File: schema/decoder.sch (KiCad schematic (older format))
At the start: 19 parts, among them Q1 BC177, U1 7402, U2 HEF4526B, U3 TLC555

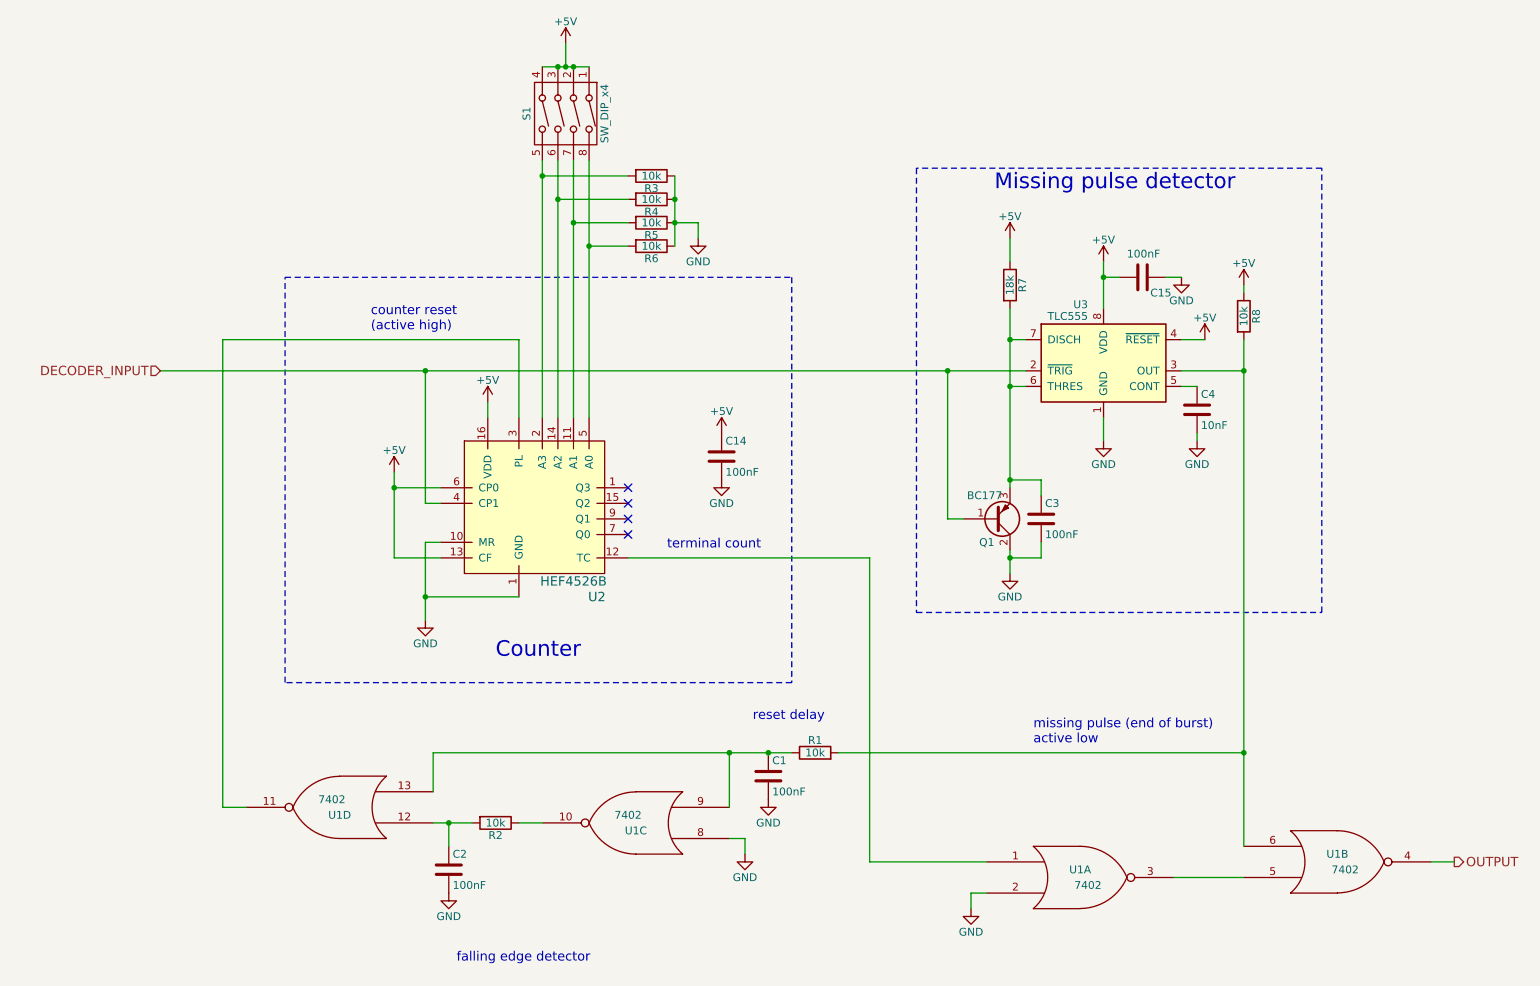
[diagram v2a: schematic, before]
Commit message: Add missing decoupling capacitors
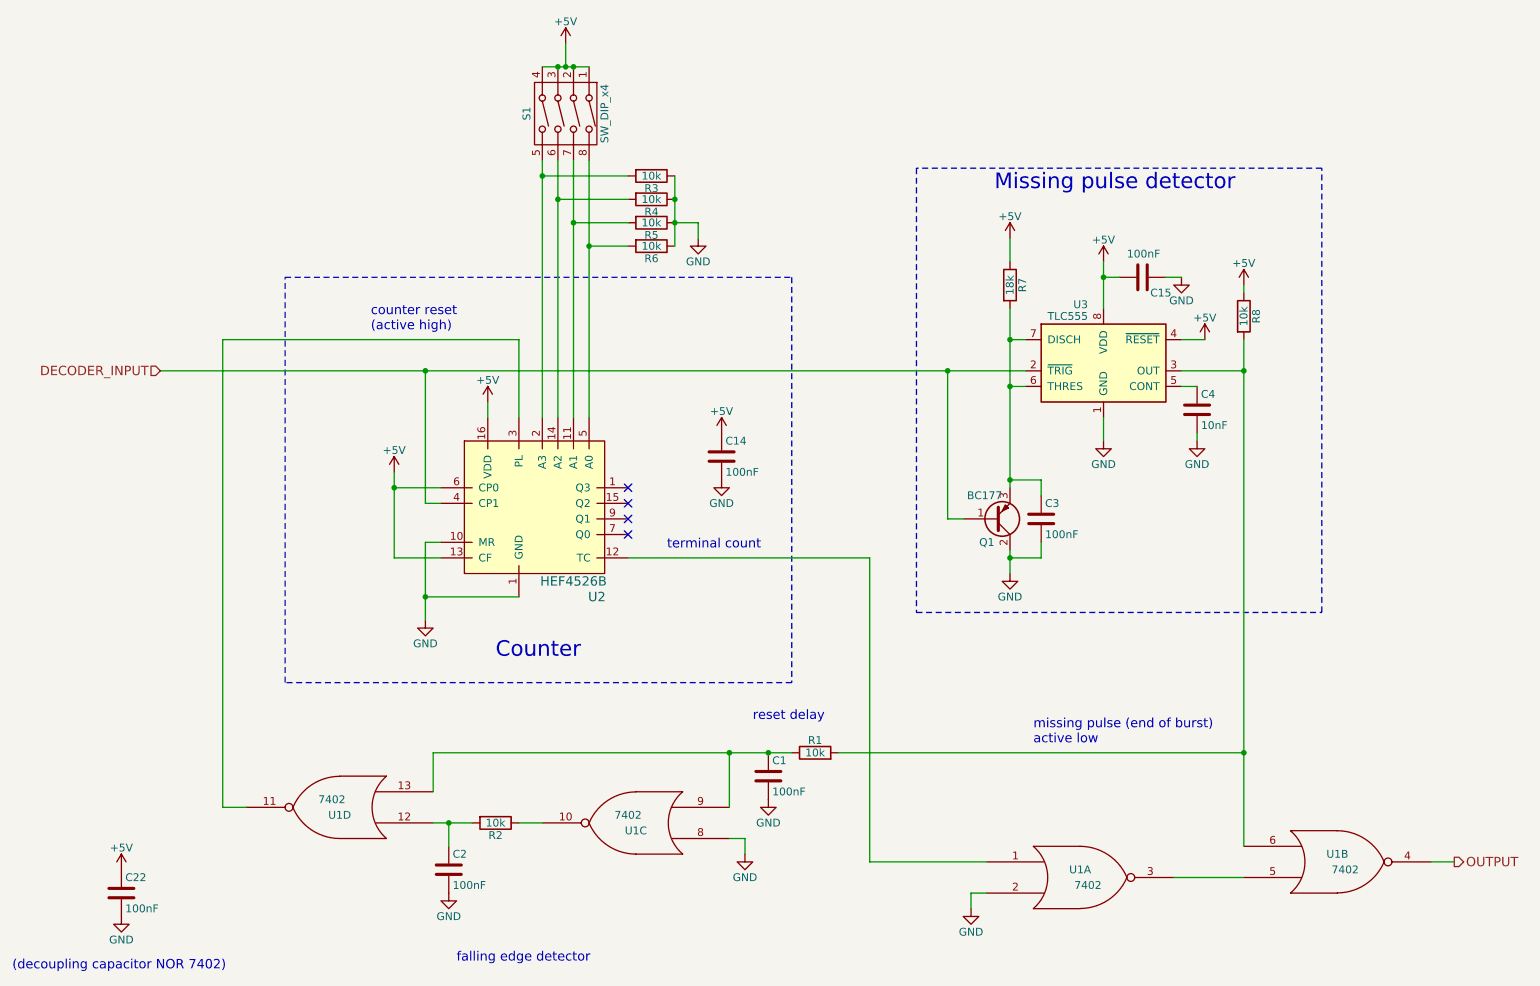
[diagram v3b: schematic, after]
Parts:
- added C22: 100nF, symbol C
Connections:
- net +5V: now also C22.1
- net GND: now also C22.2
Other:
- note added: "(decoupling capacitor NOR 7402)"
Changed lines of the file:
@@
 $EndComp
 $Comp
-L GND #PWR35
+L GND #PWR40
 U 1 1 58C0583B
 P 3350 4500
-F 0 "#PWR35" H 3350 4250 50  0001 C CNN
+F 0 "#PWR40" H 3350 4250 50  0001 C CNN
 F 1 "GND" H 3350 4350 50  0000 C CNN
 F 2 "" H 3350 4500 50  0000 C CNN
@@
 $EndComp
 $Comp
-L +5V #PWR38
+L +5V #PWR43
 U 1 1 58C05885
 P 4250 800
-F 0 "#PWR38" H 4250 650 50  0001 C CNN
+F 0 "#PWR43" H 4250 650 50  0001 C CNN
 F 1 "+5V" H 4250 940 50  0000 C CNN
 F 2 "" H 4250 800 50  0000 C CNN
@@
 $EndComp
 $Comp
-L GND #PWR44
+L GND #PWR49
 U 1 1 58C05E32
 P 6850 6350
-F 0 "#PWR44" H 6850 6100 50  0001 C CNN
+F 0 "#PWR49" H 6850 6100 50  0001 C CNN
 F 1 "GND" H 6850 6200 50  0000 C CNN
 F 2 "" H 6850 6350 50  0000 C CNN
@@
 $EndComp
 $Comp
-L GND #PWR48
+L GND #PWR53
 U 1 1 58C061DE
 P 7700 3350
-F 0 "#PWR48" H 7700 3100 50  0001 C CNN
+F 0 "#PWR53" H 7700 3100 50  0001 C CNN
 F 1 "GND" H 7700 3200 50  0000 C CNN
 F 2 "" H 7700 3350 50  0000 C CNN
@@
 $EndComp
 $Comp
-L GND #PWR46
+L GND #PWR51
 U 1 1 58C0698F
 P 7100 4200
-F 0 "#PWR46" H 7100 3950 50  0001 C CNN
+F 0 "#PWR51" H 7100 3950 50  0001 C CNN
 F 1 "GND" H 7100 4050 50  0000 C CNN
 F 2 "" H 7100 4200 50  0000 C CNN
@@
 $EndComp
 $Comp
-L GND #PWR50
+L GND #PWR55
 U 1 1 58C06B39
 P 8300 3350
-F 0 "#PWR50" H 8300 3100 50  0001 C CNN
+F 0 "#PWR55" H 8300 3100 50  0001 C CNN
 F 1 "GND" H 8300 3200 50  0000 C CNN
 F 2 "" H 8300 3350 50  0000 C CNN
@@
 $EndComp
 $Comp
-L GND #PWR42
+L GND #PWR47
 U 1 1 58C07F5B
 P 5400 6000
-F 0 "#PWR42" H 5400 5750 50  0001 C CNN
+F 0 "#PWR47" H 5400 5750 50  0001 C CNN
 F 1 "GND" H 5400 5850 50  0000 C CNN
 F 2 "" H 5400 6000 50  0000 C CNN
@@
 $EndComp
 $Comp
-L GND #PWR36
+L GND #PWR41
 U 1 1 58C08807
 P 3500 6250
-F 0 "#PWR36" H 3500 6000 50  0001 C CNN
+F 0 "#PWR41" H 3500 6000 50  0001 C CNN
 F 1 "GND" H 3500 6100 50  0000 C CNN
 F 2 "" H 3500 6250 50  0000 C CNN
@@
 $EndComp
 $Comp
-L GND #PWR43
+L GND #PWR48
 U 1 1 58C08D75
 P 5550 5650
-F 0 "#PWR43" H 5550 5400 50  0001 C CNN
+F 0 "#PWR48" H 5550 5400 50  0001 C CNN
 F 1 "GND" H 5550 5500 50  0000 C CNN
 F 2 "" H 5550 5650 50  0000 C CNN
@@
 $EndComp
 $Comp
-L +5V #PWR34
+L +5V #PWR39
 U 1 1 58C8FF2B
 P 3150 3550
-F 0 "#PWR34" H 3150 3400 50  0001 C CNN
+F 0 "#PWR39" H 3150 3400 50  0001 C CNN
 F 1 "+5V" H 3150 3690 50  0000 C CNN
 F 2 "" H 3150 3550 50  0000 C CNN
@@
 $EndComp
 $Comp
-L +5V #PWR37
+L +5V #PWR42
 U 1 1 58C9031F
 P 3750 3100
-F 0 "#PWR37" H 3750 2950 50  0001 C CNN
+F 0 "#PWR42" H 3750 2950 50  0001 C CNN
 F 1 "+5V" H 3750 3240 50  0000 C CNN
 F 2 "" H 3750 3100 50  0000 C CNN
@@
 $EndComp
 $Comp
-L GND #PWR39
+L GND #PWR44
 U 1 1 58C90F7F
 P 5100 2050
-F 0 "#PWR39" H 5100 1800 50  0001 C CNN
+F 0 "#PWR44" H 5100 1800 50  0001 C CNN
 F 1 "GND" H 5100 1900 50  0000 C CNN
 F 2 "" H 5100 2050 50  0000 C CNN
@@
 NoConn ~ 4650 3950
 $Comp
-L +5V #PWR45
+L +5V #PWR50
 U 1 1 58C91824
 P 7100 2050
-F 0 "#PWR45" H 7100 1900 50  0001 C CNN
+F 0 "#PWR50" H 7100 1900 50  0001 C CNN
 F 1 "+5V" H 7100 2190 50  0000 C CNN
 F 2 "" H 7100 2050 50  0000 C CNN
@@
 $EndComp
 $Comp
-L +5V #PWR47
+L +5V #PWR52
 U 1 1 58C91A38
 P 7700 2200
-F 0 "#PWR47" H 7700 2050 50  0001 C CNN
+F 0 "#PWR52" H 7700 2050 50  0001 C CNN
 F 1 "+5V" H 7700 2340 50  0000 C CNN
 F 2 "" H 7700 2200 50  0000 C CNN
@@
 $EndComp
 $Comp
-L +5V #PWR52
+L +5V #PWR57
 U 1 1 58C91BDC
 P 8600 2350
-F 0 "#PWR52" H 8600 2200 50  0001 C CNN
+F 0 "#PWR57" H 8600 2200 50  0001 C CNN
 F 1 "+5V" H 8600 2490 50  0000 C CNN
 F 2 "" H 8600 2350 50  0000 C CNN
@@
 $EndComp
 $Comp
-L GND #PWR41
+L GND #PWR46
 U 1 1 593E7289
 P 5250 3600
-F 0 "#PWR41" H 5250 3350 50  0001 C CNN
+F 0 "#PWR46" H 5250 3350 50  0001 C CNN
 F 1 "GND" H 5250 3450 50  0000 C CNN
 F 2 "" H 5250 3600 50  0000 C CNN
@@
 	8600 2350 8600 2400
 Wire Wire Line
-	7700 2200 7700 2300
-Wire Wire Line
-	7700 2300 7700 2500
+	7700 2200 7700 2500
 Wire Wire Line
 	7100 2050 7100 2200
@@
 Connection ~ 4950 1800
 Wire Wire Line
-	4950 1650 4950 1800
-Wire Wire Line
-	4950 1800 4950 1950
-Wire Wire Line
-	4950 1950 4950 2100
+	4950 1650 4950 2100
 Connection ~ 4400 2100
 Wire Wire Line
@@
 	4650 1950 4300 1950
 Wire Wire Line
-	4400 1550 4400 2100
-Wire Wire Line
-	4400 2100 4400 3200
-Wire Wire Line
-	4300 1550 4300 1950
-Wire Wire Line
-	4300 1950 4300 3200
+	4400 1550 4400 3200
+Wire Wire Line
+	4300 1550 4300 3200
 Connection ~ 4200 1800
 Wire Wire Line
@@
 	4650 1650 4100 1650
 Wire Wire Line
-	4100 950  4200 950
-Wire Wire Line
-	4200 950  4250 950
-Wire Wire Line
-	4250 950  4300 950
-Wire Wire Line
-	4300 950  4400 950
+	4100 950  4400 950
 Connection ~ 4250 950
 Wire Wire Line
@@
 	5550 5650 5550 5650
 Wire Wire Line
-	3400 5350 5300 5350
-Wire Wire Line
-	5300 5350 5550 5350
-Wire Wire Line
-	5550 5350 5700 5350
+	3400 5350 5700 5350
 Wire Wire Line
 	3400 5350 3400 5600
@@
 	3500 5800 3500 5950
 Wire Wire Line
-	3400 5800 3500 5800
-Wire Wire Line
-	3500 5800 3650 5800
+	3400 5800 3650 5800
 Wire Wire Line
 	3950 5800 4100 5800
@@
 Connection ~ 8600 2900
 Wire Wire Line
-	8600 2700 8600 2900
-Wire Wire Line
-	8600 2900 8600 5350
-Wire Wire Line
-	8600 5350 8600 5950
+	8600 2700 8600 5950
 Wire Wire Line
 	8200 2900 8600 2900
@@
 Connection ~ 7100 4100
 Wire Wire Line
-	7100 4050 7100 4100
-Wire Wire Line
-	7100 4100 7100 4200
+	7100 4050 7100 4200
 Wire Wire Line
 	7300 4100 7100 4100
@@
 	7100 3000 7200 3000
 Wire Wire Line
-	7100 2500 7100 2700
-Wire Wire Line
-	7100 2700 7100 3000
-Wire Wire Line
-	7100 3000 7100 3600
-Wire Wire Line
-	7100 3600 7100 3650
+	7100 2500 7100 3650
 Wire Wire Line
 	3350 3750 3350 2900
@@
 	6700 3850 6800 3850
 Wire Wire Line
-	1650 2900 3350 2900
-Wire Wire Line
-	3350 2900 6700 2900
-Wire Wire Line
-	6700 2900 7200 2900
+	1650 2900 7200 2900
 Wire Wire Line
 	6700 2900 6700 3850
@@
 	3950 4350 3350 4350
 Wire Wire Line
-	3350 4000 3350 4350
-Wire Wire Line
-	3350 4350 3350 4500
+	3350 4000 3350 4500
 Wire Wire Line
 	3450 4000 3350 4000
@@
 	3150 4100 3450 4100
 Wire Wire Line
-	3150 3550 3150 3650
-Wire Wire Line
-	3150 3650 3150 4100
+	3150 3550 3150 4100
 Wire Wire Line
 	3450 3650 3150 3650
@@
 Connection ~ 4200 950
 Wire Wire Line
-	4200 1550 4200 1800
-Wire Wire Line
-	4200 1800 4200 3200
-Wire Wire Line
-	4100 1550 4100 1650
-Wire Wire Line
-	4100 1650 4100 3200
+	4200 1550 4200 3200
+Wire Wire Line
+	4100 1550 4100 3200
 Wire Wire Line
 	2050 5700 2050 2700
@@
 	6000 5350 8600 5350
 $Comp
-L +5V #PWR40
+L +5V #PWR45
 U 1 1 593E76EB
 P 5250 3300
-F 0 "#PWR40" H 5250 3150 50  0001 C CNN
+F 0 "#PWR45" H 5250 3150 50  0001 C CNN
 F 1 "+5V" H 5250 3440 50  0000 C CNN
 F 2 "" H 5250 3300 50  0000 C CNN
@@
 $EndComp
 $Comp
-L GND #PWR49
+L GND #PWR54
 U 1 1 593E7B88
 P 8200 2300
-F 0 "#PWR49" H 8200 2050 50  0001 C CNN
+F 0 "#PWR54" H 8200 2050 50  0001 C CNN
 F 1 "GND" H 8200 2150 50  0000 C CNN
 F 2 "" H 8200 2300 50  0000 C CNN
@@
 Connection ~ 7700 2300
 $Comp
-L +5V #PWR51
+L +5V #PWR56
 U 1 1 593E8724
 P 8350 2700
-F 0 "#PWR51" H 8350 2550 50  0001 C CNN
+F 0 "#PWR56" H 8350 2550 50  0001 C CNN
 F 1 "+5V" H 8350 2840 50  0000 C CNN
 F 2 "" H 8350 2700 50  0000 C CNN
@@
 	1    0    0    -1
 $EndComp
+$Comp
+L C C22
+U 1 1 593ECAC0
+P 1400 6250
+F 0 "C22" H 1425 6350 50  0000 L CNN
+F 1 "100nF" H 1425 6150 50  0000 L CNN
+F 2 "" H 1438 6100 50  0000 C CNN
+F 3 "" H 1400 6250 50  0000 C CNN
+	1    1400 6250
+	1    0    0    -1
+$EndComp
+$Comp
+L GND #PWR38
+U 1 1 593ECAC6
+P 1400 6400
+F 0 "#PWR38" H 1400 6150 50  0001 C CNN
+F 1 "GND" H 1400 6250 50  0000 C CNN
+F 2 "" H 1400 6400 50  0000 C CNN
+F 3 "" H 1400 6400 50  0000 C CNN
+	1    1400 6400
+	1    0    0    -1
+$EndComp
+$Comp
+L +5V #PWR37
+U 1 1 593ECACC
+P 1400 6100
+F 0 "#PWR37" H 1400 5950 50  0001 C CNN
+F 1 "+5V" H 1400 6240 50  0000 C CNN
+F 2 "" H 1400 6100 50  0000 C CNN
+F 3 "" H 1400 6100 50  0000 C CNN
+	1    1400 6100
+	1    0    0    -1
+$EndComp
+Text Notes 700  6750 0    60   ~ 0
+(decoupling capacitor NOR 7402)
 $EndSCHEMATC
